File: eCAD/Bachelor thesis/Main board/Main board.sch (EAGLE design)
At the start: 65 parts, among them IC1 BC660K-GL, IC2 TP4056X, IC3 DW01A-G, IC4 ME6211C33M5G-N, IC5 ME6211C33M5G-N, IC6 ESP32-WROOM-32E_M113EH3200PH3Q, Q1 IRF7319TRPBF, Q2 IRF7319TRPBF, Q3 SI2347DS-T1-GE3, Q4 FS8205A

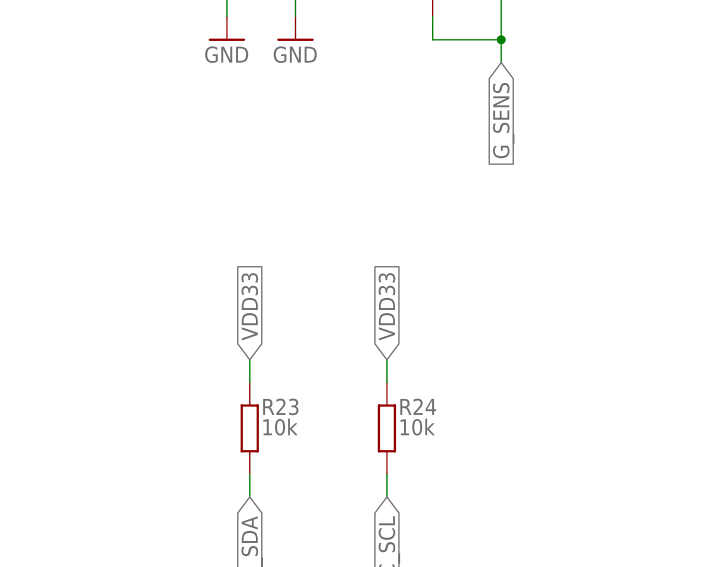
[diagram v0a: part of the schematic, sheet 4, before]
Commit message: I2C pull-up Rs added on switched source
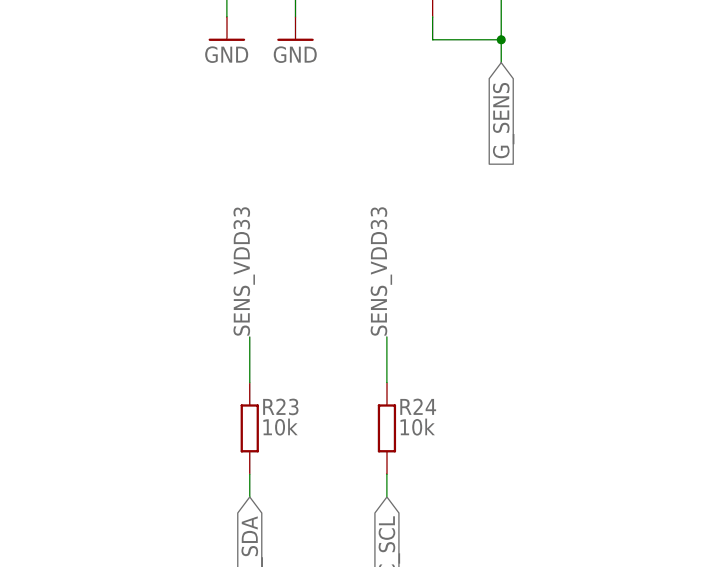
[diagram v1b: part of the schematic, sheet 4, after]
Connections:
- net SENS_VDD33: now also R23.2, R24.2
- net VDD33: no longer R23.2, R24.2
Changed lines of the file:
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@@
 <setting verticaltext="up"/>
 </settings>
-<grid distance="0.1" unitdist="inch" unit="mil" style="lines" multiple="1" display="yes" altdistance="0.01" altunitdist="inch" altunit="mil"/>
+<grid distance="0.1" unitdist="inch" unit="inch" style="lines" multiple="1" display="no" altdistance="0.01" altunitdist="inch" altunit="inch"/>
 <layers>
 <layer number="1" name="Top" color="4" fill="1" visible="no" active="no"/>
@@
 <label x="200.66" y="121.92" size="1.778" layer="95" rot="R180"/>
 </segment>
-<segment>
-<pinref part="R23" gate="G$1" pin="2"/>
-<wire x1="38.1" y1="35.56" x2="38.1" y2="38.1" width="0.1524" layer="91"/>
-<label x="38.1" y="38.1" size="1.778" layer="95" rot="R90" xref="yes"/>
-</segment>
-<segment>
-<pinref part="R24" gate="G$1" pin="2"/>
-<wire x1="53.34" y1="35.56" x2="53.34" y2="38.1" width="0.1524" layer="91"/>
-<label x="53.34" y="38.1" size="1.778" layer="95" rot="R90" xref="yes"/>
-</segment>
 </net>
 <net name="ESP_PIN" class="0">
@@
 <label x="200.66" y="78.74" size="1.778" layer="95" rot="R180"/>
 </segment>
-</net>
+<segment>
+<pinref part="R23" gate="G$1" pin="2"/>
+<wire x1="38.1" y1="35.56" x2="38.1" y2="40.64" width="0.1524" layer="91"/>
+<label x="38.1" y="40.64" size="1.778" layer="95" rot="R90"/>
+</segment>
+<segment>
+<pinref part="R24" gate="G$1" pin="2"/>
+<wire x1="53.34" y1="35.56" x2="53.34" y2="40.64" width="0.1524" layer="91"/>
+<label x="53.34" y="40.64" size="1.778" layer="95" rot="R90"/>
+</segment>
+</net>

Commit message: Work around Quectel BC660K NB-IoT module
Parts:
- removed C18: 220u, rcl:CPOL-EUD
- removed C19: 100n, rcl:C-EUC0805
- removed C20: 22p, rcl:C-EUC0805
- removed C21: 100p, rcl:C-EUC0805
- removed R25, R26: 10K, rcl:R-EU_R0805
- removed SJ5: (no value), jumper:SJ
- removed U$1: USBC-6P, USBC6P:USBC-6P
- added C12, C14, C2: 1u, rcl:C-EUC0805
- added C15, C3: 100n, rcl:C-EUC0805
- added LED1: STAT1, led:LEDCHIPLED_0805
- added Q5, Q6: IRF7319TRPBF, 1-component-search:IRF7319TRPBF
- added R1, R2: 10K, rcl:R-EU_R0805
- added R11: 100R, rcl:R-EU_R0805
- added SJ2: (no value), jumper:SJ
- added TP1, TP2: TPB2,54, testpad:TPB2,54
- added USBC: USBC-6P, USBC6P:USBC-6P
- C10: value 100n -> 10u
- C4: value 1u -> 220u; device rcl:C-EUC0805 -> rcl:CPOL-EUD
- C6: value 10u -> 22p
- C7: value 100n -> 100p
- C8, C9: value 1u -> 100n
- IC1: value BC660K-GL -> ESP32-WROOM-32E_M113EH3200PH3Q; device 1-component-search:BC660K-GL -> 1-component-search:ESP32-WROOM-32E_M113EH3200PH3Q
- IC2: value TP4056X -> BC660K-GL; device TP4056X:TP4056X -> 1-component-search:BC660K-GL
- IC4: value ME6211C33M5G-N -> TP4056X; device 1-component-search:ME6211C33M5G-N -> TP4056X:TP4056X
- IC6: value ESP32-WROOM-32E_M113EH3200PH3Q -> ME6211C33M5G-N; device 1-component-search:ESP32-WROOM-32E_M113EH3200PH3Q -> 1-component-search:ME6211C33M5G-N
- Q1, Q2: value IRF7319TRPBF -> PDTC114EU,115; device 1-component-search:IRF7319TRPBF -> PDTC114EU_115:PDTC114EU,115
- Q3: value SI2347DS-T1-GE3 -> FS8205A; device 1-component-search:SI2347DS-T1-GE3 -> 1-component-search:FS8205A
- Q4: value FS8205A -> SI2347DS-T1-GE3; device 1-component-search:FS8205A -> 1-component-search:SI2347DS-T1-GE3
- R10, R9: value 10k -> 5k1
- R12: value Rprog -> 10k
- R13: value 100R -> Rprog
- R14: value 1k -> 10k
- R18, R19: value 5k1 -> 10k
- R20: value 1M -> 10k
- R21: value 4k7 -> 10k
- R22: value 10K -> 4k7
- R5: value 10k -> 10K
- R6: value 10k -> 2k2; device rcl:R-EU_R0805 -> rcl:R-EU_R1206
- R7: value 10k -> 1M
- R8: value 10k -> 1k
- renumbered BAT_IN to JP4, C16 to C13, C17 to C1, DS18B20 to J3, ESP_BOOT1 to S2, ESP_EN1 to JP1, ESP_RESET1 to S1, FAN to JP5, I2C to J4, NB_BOOT1 to S4, NB_PSM1 to S5, NB_RESET1 to S3, R23 to R16, R24 to R17, RAIN_GAUGE to J2, SJ4 to SJ1, SOLAR_IN to J1
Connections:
- new net BOOT: IC2.BOOT
- new net N$1: IC2.DBG_RXD, TP1.TP
- new net N$16: LED1.C, R6.2
- new net N$17: Q2.OUTPUT, R6.1
- new net N$2: IC2.DBG_TXD, TP2.TP
- new net NETLIGHT: IC2.NETLIGHT, Q2.INPUT
- new net PSM_EINT: IC2.PSM_EINT
- new net RESET_N: C8.1, IC2.RESET_N, Q1.OUTPUT
- new net RESET_QUECTEL: Q1.INPUT
- net !CHRG: now also IC4.!CHRG; no longer IC2.!CHRG
- net !STDBY: now also IC4.!STDBY; no longer IC2.!STDBY
- net BAT+: now also IC4.BAT, Q4.D, Q5.S2, R11.2, R18.1; no longer IC2.BAT, Q1.S2, Q3.D, R13.2, R6.1
- net BAT-: now also C9.2, Q3.S1_1, Q3.S1_2; no longer C7.2, Q4.S1_1, Q4.S1_2
- net BOOT_N: now also IC1.IO19, R4.2; no longer IC6.IO19, R25.2
- net DS18B_SIG: now also IC1.IO32, R22.1; no longer IC6.IO32, R21.1
- net ESP_EN: now also C2.1, IC1.EN, R1.1; no longer C4.1, IC6.EN, R3.1
- net ESP_FLASH: now also IC1.IO0, R2.1; no longer IC6.IO0, R4.1
- net ESP_PIN: now also IC1.IO33, Q5.G1, Q6.G1, R14.2, R15.2; no longer IC6.IO33, Q1.G1, Q2.G1, R5.2, R9.2
- net FLASH_RX: now also IC1.RXD0; no longer IC6.RXD0
- net FLASH_TX: now also IC1.TXD0; no longer IC6.TXD0
- net GND: now also C12.2, C14.2, C15.2, C2.2, C3.1, C4.-, C5.2, C7.2, IC1.GND_1, IC1.GND_10, IC1.GND_11, IC1.GND_12, IC1.GND_2, IC1.GND_3, IC1.GND_4, IC1.GND_5, IC1.GND_6, IC1.GND_7, IC1.GND_8, IC1.GND_9, IC2.GND_1, IC2.GND_10, IC2.GND_2, IC2.GND_3, IC2.GND_4, IC2.GND_5, IC2.GND_6, IC2.GND_7, IC2.GND_8, IC2.GND_9, IC2.VIO_SEL, IC4.EAD, IC4.GND, IC4.TEMP, IC6.VSS, Q1.GND, Q2.GND, Q3.S2_1, Q3.S2_2, Q5.S1, Q6.S1, R10.1, R12.1, R13.2, R21.1, R3.1, R4.1, R7.2, USBC.GND; no longer C18.-, C19.2, C20.2, C21.2, C4.2, C5.1, C9.2, IC2.EAD, IC2.GND, IC2.TEMP, IC4.VSS, IC6.GND_1, IC6.GND_10, IC6.GND_11, IC6.GND_12, IC6.GND_2, IC6.GND_3, IC6.GND_4, IC6.GND_5, IC6.GND_6, IC6.GND_7, IC6.GND_8, IC6.GND_9, Q1.S1, Q2.S1, Q4.S2_1, Q4.S2_2, R12.2, R18.1, R19.1, R20.2, R22.1, R25.1, R26.1, U$1.GND
- net G_BAT: now also Q5.D1_2, Q5.G2, R18.2; no longer Q1.D1_2, Q1.G2, R6.2
- net G_SENS: now also Q6.D1_2, Q6.G2, R19.2; no longer Q2.D1_2, Q2.G2, R10.2
- net I2C_SCL: now also IC1.IO22; no longer IC6.IO22
- net I2C_SDA: now also IC1.IO21; no longer IC6.IO21
- net N$10: now also Q3.G1; no longer Q4.G1
- net N$11: now also R9.2, USBC.CC2; no longer R19.2, U$1.CC2
- net N$12: now also Q3.G2; no longer Q4.G2
- net N$13: now also R10.2, USBC.CC1; no longer R18.2, U$1.CC1
- net N$14: now also R7.1, USBC.S; no longer R20.1, U$1.S
- net N$15: now also Q5.D2_1, R20.2; no longer Q1.D2_1, R7.2
- net N$3: now also IC1.IO16, SJ2.1; no longer IC6.IO16, SJ3.1
- net N$4: now also IC1.IO17; no longer IC6.IO17
- net N$5: now also IC4.PROG, R13.1; no longer IC2.PROG, R12.1
- net N$7: now also C9.1, R11.1; no longer C7.1, R13.1
- net N$8: now also D1.A, SJ3.1, USBC.VBUS; no longer D2.A, SJ5.1, U$1.VBUS
- net N$9: now also R8.2; no longer R14.2
- net OUT+: now also C12.1, D2.K, IC6.CE, IC6.VIN, Q4.S; no longer C8.1, D1.K, IC4.CE, IC4.VIN, Q3.S
- net PSM_EINT_N: now also IC1.IO5, R5.2; no longer IC6.IO5, R26.2
- net RAIN_GAUGE_INPUT: now also IC1.IO4; no longer IC6.IO4
- net RAIN_SENS: now also IC1.IO35; no longer IC6.IO35
- net RESET_EN: now also IC1.IO18, R3.2; no longer IC6.IO18, R22.2
- net SENS_VDD33: now also Q6.D2_1, R22.2; no longer Q2.D2_1, R21.2
- net UART_MCU_RX: now also IC2.MAIN_TXD, SJ2.2; no longer SJ3.2
- net UART_MCU_TX: now also IC2.MAIN_RXD
- net VDD33: now also C14.1, C3.2, C4.+, C5.1, C6.1, C7.1, IC1.3V3, IC2.VBAT_1, IC2.VBAT_2, IC6.VOUT, LED1.A, Q6.S2, R1.2, R19.1, R2.2; no longer C18.+, C19.1, C20.1, C21.1, C5.2, C9.1, IC4.VOUT, IC6.3V3, Q2.S2, R10.1, R3.2, R4.2
- net VIN: now also C10.1, D1.K, D2.A, IC4.CE, IC4.VCC, Q4.G, R12.2, SJ3.2; no longer C6.1, D1.A, D2.K, IC2.CE, IC2.VCC, Q3.G, R15.2, SJ5.2
- net VOL_SENS: now also C15.1, IC1.IO34, R20.1, R21.2; no longer C10.1, IC6.IO34, R7.1, R8.2
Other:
- note added: "TVS diode?"
- note added: "VIO_SEL grounded for 3.3V logic levels"

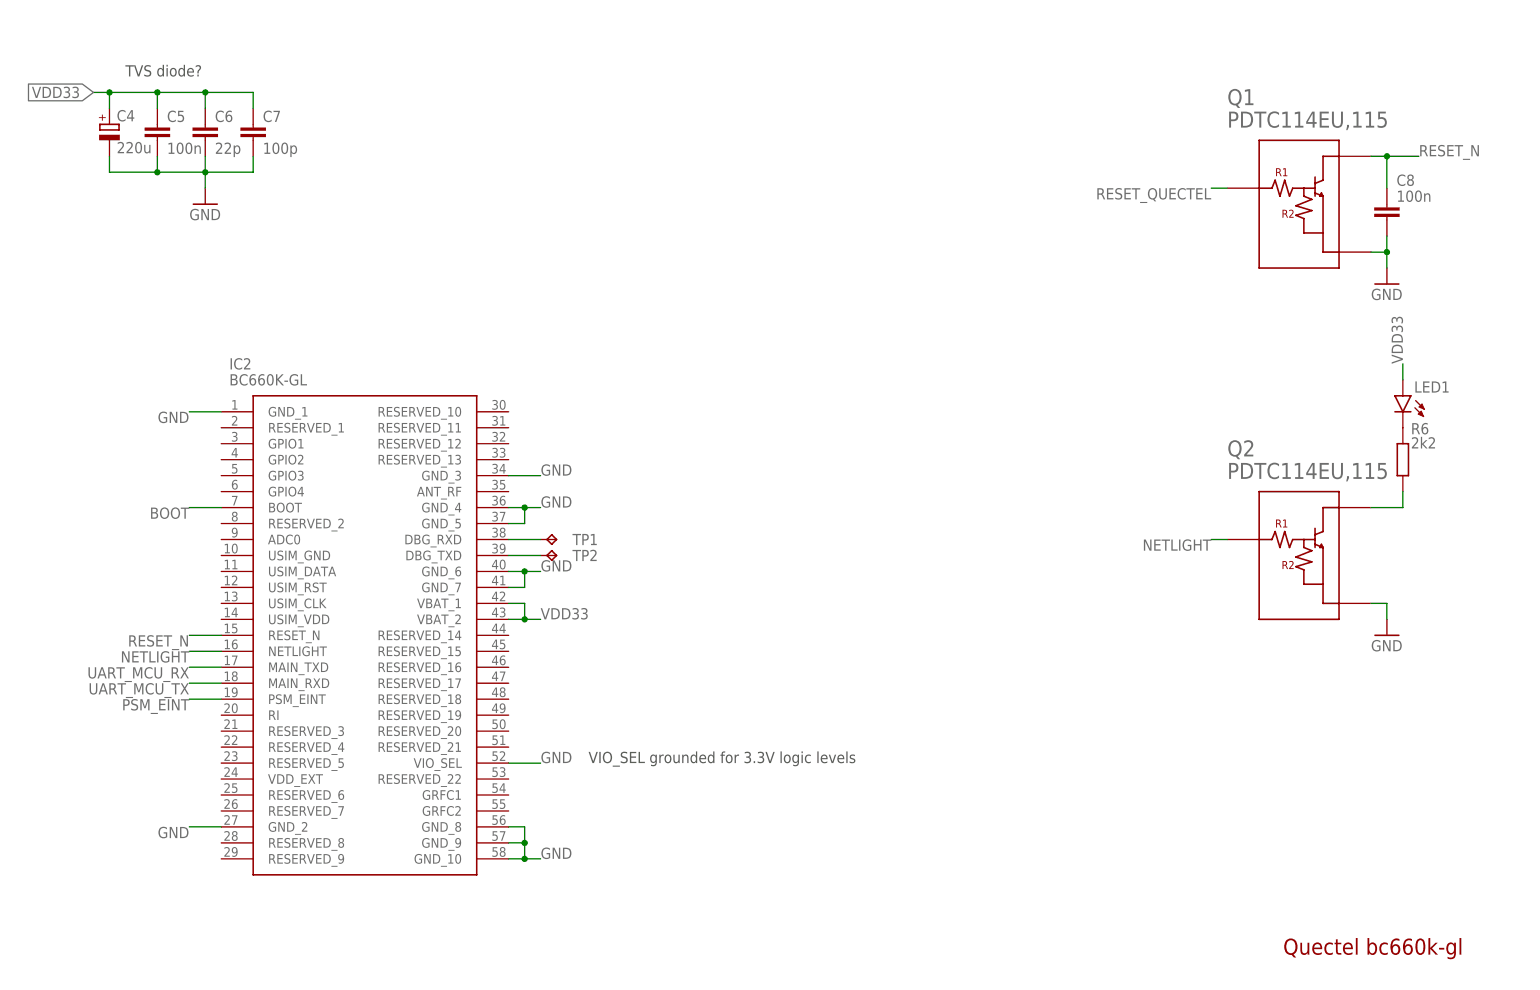
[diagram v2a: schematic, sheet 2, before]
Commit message: Work around Quectel BC660K-GL module
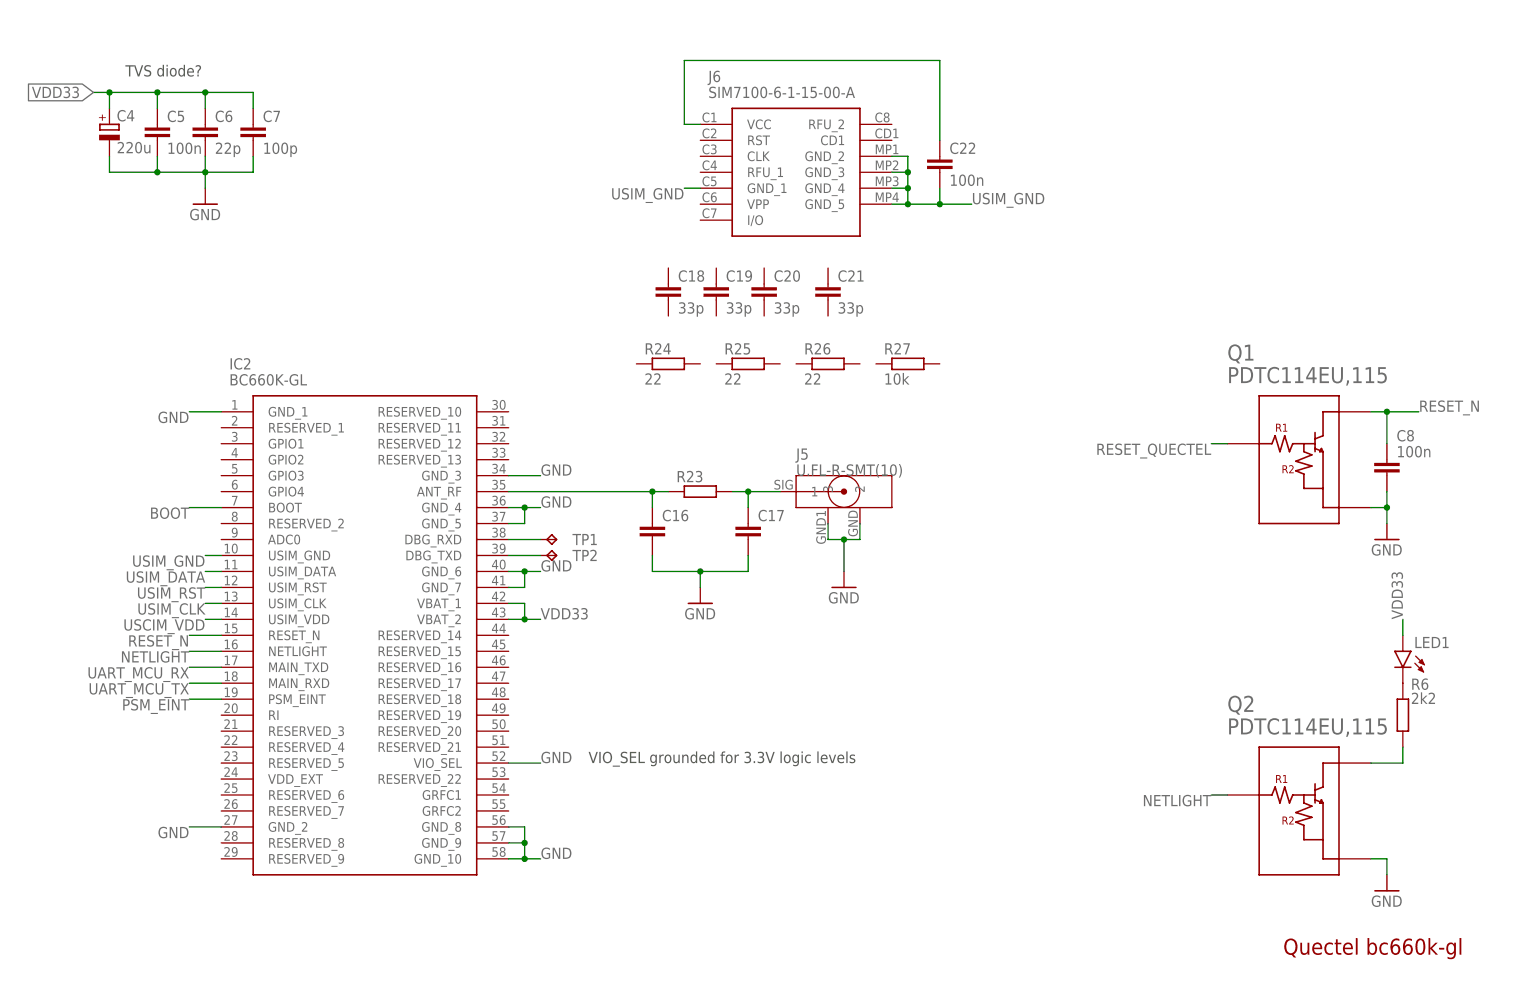
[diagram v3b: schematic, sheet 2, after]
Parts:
- added C16, C17: (no value), rcl:C-EUC0805
- added C18, C19, C20, C21: 33p, rcl:C-EUC0805
- added C22: 100n, rcl:C-EUC0805
- added J5: U.FL-R-SMT(10), Connectors:U.FL-R-SMT(10)
- added J6: SIM7100-6-1-15-00-A, 1-component-search:SIM7100-6-1-15-00-A
- added R23: (no value), rcl:R-EU_R0805
- added R24, R25, R26: 22, rcl:R-EU_R0805
- added R27: 10k, rcl:R-EU_R0805
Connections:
- new net N$18: C22.1, J6.VCC
- new net N$19: C16.1, IC2.ANT_RF, R23.1
- new net N$20: C17.1, J5.1, R23.2
- new net USCIM_VDD: IC2.USIM_VDD
- new net USIM_CLK: IC2.USIM_CLK
- new net USIM_DATA: IC2.USIM_DATA
- new net USIM_GND: C22.2, IC2.USIM_GND, J6.GND_1, J6.GND_2, J6.GND_3, J6.GND_4, J6.GND_5
- new net USIM_RST: IC2.USIM_RST
- net GND: now also C16.2, C17.2, J5.2, J5.3
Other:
- moved on the sheet: C8, LED1, Q1, Q2, R6

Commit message: Completed antena interface, power circuitry
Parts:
- removed Q5, Q6: IRF7319TRPBF, 1-component-search:IRF7319TRPBF
- removed USBC: USBC-6P, USBC6P:USBC-6P
- added $3_24_$_2023-03-17_12-09-30: USBC-6P, USBC6P:USBC-6P
- added $3_25_$_2023-03-17_12-09-30: BLOSSOM-BLM-18650-1PCS, battery-holders:BLOSSOM-BLM-18650-1PCS
- added C23: 1u, rcl:C-EUC0805
- added C24, C27, C28: 100n, rcl:C-EUC0805
- added C25: 50, rcl:CPOL-EUE5-10.5
- added C26: 22u, rcl:C-EUC0805
- added D3, D4: PMEG2010EJ,115, 1-component-search:PMEG2010EJ,115
- added D5: SMBJ6.5A, 1-component-search:SMBJ6.5A
- added HM1: BME280, 1-component-search:BME280
- added IC10, IC9: SMS3.3.TCT, 1-component-search:SMS3.3.TCT
- added IC7, IC8: ME6211C33M5G-N, 1-component-search:ME6211C33M5G-N
- added JP7: FAN, jumper:JP2E
- added LED2: !PG, led:LEDCHIPLED_0805
- added LED3: STAT2, led:LEDCHIPLED_0805
- added LED4: STAT1, led:LEDCHIPLED_0805
- added R28, R29, R33, R34, R35, R36: 10k, rcl:R-EU_R0805
- added R30, R31, R32: 4k7, rcl:R-EU_R0805
- added SJ4: (no value), jumper:SJ
- added SJ5: (no value), jumper:SJ2W
- C1, C4: value 220u -> 470u
- C10: value 10u -> 33p
- C11, C13: value 1u -> 33p
- C12: value 1u -> (none)
- C14: value 1u -> 100n
- C16: value (none) -> 100n
- C17: value (none) -> 10u
- C18, C21: value 33p -> 4u7
- C19, C20: value 33p -> 1u
- C22: value 100n -> 1u
- C8: value 100n -> 33p
- C9: value 100n -> (none)
- D1, D2: value 1N4148WS-7-F -> SMBJ6.5A; device 1-component-search:1N4148WS-7-F -> 1-component-search:SMBJ6.5A
- IC3: value DW01A-G -> SMS3.3.TCT; device 1-component-search:DW01A-G -> 1-component-search:SMS3.3.TCT
- IC4: value TP4056X -> AP9101CK6-ADTRG1; device TP4056X:TP4056X -> 1-component-search:AP9101CK6-ADTRG1
- IC5: value ME6211C33M5G-N -> FDS6898A; device 1-component-search:ME6211C33M5G-N -> 1-component-search:FDS6898A
- IC6: value ME6211C33M5G-N -> MCP73871-2CCI_ML; device 1-component-search:ME6211C33M5G-N -> 1-component-search:MCP73871-2CCI_ML
- J1: value XT30PW-M -> U.FL-R-SMT(10); device 1-component-search:XT30PW-M -> Connectors:U.FL-R-SMT(10)
- J2: value RJE01-660-01 -> SIM7100-6-1-15-00-A; device 1-component-search:RJE01-660-01 -> 1-component-search:SIM7100-6-1-15-00-A
- J3: value RJE01-660-01 -> XT30PW-M; device 1-component-search:RJE01-660-01 -> 1-component-search:XT30PW-M
- J5: value U.FL-R-SMT(10) -> RJE01-660-01; device Connectors:U.FL-R-SMT(10) -> 1-component-search:RJE01-660-01
- J6: value SIM7100-6-1-15-00-A -> RJE01-660-01; device 1-component-search:SIM7100-6-1-15-00-A -> 1-component-search:RJE01-660-01
- JP2: value UART_FLASH -> ESP_UART; device pinhead:PINHD-1X4 -> jumper:JP4E
- JP3: value UART_NB -> NB_UART; device pinhead:PINHD-1X4 -> jumper:JP4E
- JP4: value (none) -> NTC; device pinhead:PINHD-1X2 -> jumper:JP1E
- JP5: value (none) -> LED_VDD; device pinhead:PINHD-1X3 -> jumper:JP1E
- Q3: value FS8205A -> IRF7319TRPBF; device 1-component-search:FS8205A -> 1-component-search:IRF7319TRPBF
- Q4: value SI2347DS-T1-GE3 -> IRF7319TRPBF; device 1-component-search:SI2347DS-T1-GE3 -> 1-component-search:IRF7319TRPBF
- R10: value 5k1 -> (none)
- R11: value 100R -> 2k2; device rcl:R-EU_R0805 -> rcl:R-EU_R1206
- R12: value 10k -> 2k7
- R13: value Rprog -> 1M
- R14, R15: value 10k -> 5k1
- R16: value 10k -> 330R
- R17, R18, R27: value 10k -> (none)
- R19, R20, R21: value 10k -> 470
- R22: value 4k7 -> 10k
- R23: value (none) -> 10k
- R24: value 22 -> 10k
- R25: value 22 -> 1k
- R26: value 22 -> (none)
- R6: value 2k2 -> 10k; device rcl:R-EU_R1206 -> rcl:R-EU_R0805
- R7: value 1M -> 22
- R8: value 1k -> 22
- R9: value 5k1 -> 22
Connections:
- removed net !CHRG: IC4.!CHRG
- removed net !STDBY: IC4.!STDBY
- removed net N$10: IC3.OD, Q3.G1
- removed net N$11: R9.2, USBC.CC2
- removed net N$12: IC3.OC, Q3.G2
- removed net N$13: R10.2, USBC.CC1
- removed net N$14: R7.1, USBC.S
- removed net N$15: Q5.D2_1, R20.2
- removed net N$18: C22.1, J6.VCC
- removed net OUT+: C12.1, D2.K, IC6.CE, IC6.VIN, Q4.S
- removed net RAIN_SENS: IC1.IO35
- removed net RAIN_SENSE: J4.6
- removed net USCIM_VDD: IC2.USIM_VDD
- new net !PG: IC1.IO27, IC6.!PG, R19.2, R22.2
- new net !TE1: IC6.!TE, R25.1
- new net BAT_Q: Q3.D2_1, Q3.D2_2, R22.1, R23.1, R24.1, R35.2
- new net CC3: $3_24_$_2023-03-17_12-09-30.CC2, R15.1
- new net CC4: $3_24_$_2023-03-17_12-09-30.CC1, R14.1
- new net DRAIN1: IC5.D1_1, IC5.D1_2, IC5.D2_1, IC5.D2_2
- new net G3: IC4.DO, IC5.G1
- new net G4: IC4.CO, IC5.G2
- new net N$21: C10.1, IC3.I/O1, J2.RST, R7.2
- new net N$22: C11.1, IC3.I/O2, J2.CLK, R8.2
- new net N$23: C13.1, IC3.I/O4, J2.I/O, R9.2
- new net OUT: C18.1, IC6.OUT_1, IC6.OUT_2, SJ5.3
- new net PROG2: IC6.PROG3, R26.1
- new net PROG4: IC6.PROG1, R27.1
- new net PV_IN1: D1.K, D3.A, J3.1, SJ3.1
- new net S1: $3_24_$_2023-03-17_12-09-30.S, R13.1
- new net STAT1: IC1.IO25, IC6.STAT1/!LBO, R21.2, R24.2
- new net STAT2: IC1.IO26, IC6.STAT2, R20.2, R23.2
- new net THERM1: IC6.THERM, JP4.2
- new net USIM_VDD: C14.1, C8.1, IC2.USIM_VDD, IC3.I/O3, J2.VCC, R6.1
- new net VBAT: $3_25_$_2023-03-17_12-09-30.+, C21.1, D5.K, IC6.VBAT_1, IC6.VBAT_2, IC6.VBAT_SENSE, R16.2, SJ5.1
- new net VBUS1: $3_24_$_2023-03-17_12-09-30.VBUS, D2.K, D4.A, SJ4.1
- new net VCC: IC6.PROG2
- new net VDD_LED: JP5.1, LED1.A, LED2.A, LED3.A, LED4.A
- new net VIN_LDO: C20.1, IC8.CE, IC8.VIN, SJ5.2
- new net VM1: IC4.VM, R12.2
- new net VPCC1: IC6.VPCC, R17.1, R18.1
- net BAT+: now also Q3.S2, R33.1; no longer IC4.BAT, JP4.1, Q4.D, Q5.S2, R11.2, R18.1
- net BAT-: now also $3_25_$_2023-03-17_12-09-30.-, C16.2, IC4.VSS, IC5.S1; no longer C9.2, IC3.GND, JP4.2, Q3.S1_1, Q3.S1_2
- net DS18B_SIG: now also IC9.I/O4, J5.5, R32.1; no longer J3.2, R22.1
- net ESP_PIN: now also Q3.G1, Q4.G1, R28.2, R29.2; no longer Q5.G1, Q6.G1, R14.2, R15.2
- net GND: now also $3_24_$_2023-03-17_12-09-30.GND, C18.2, C19.2, C20.2, C21.2, C22.2, C23.2, C24.2, C25.-, C26.1, C27.1, C28.2, C9.2, D1.A, D2.A, D5.A, HM1.GND_1, HM1.GND_2, HM1.SDO, IC10.GND_1, IC10.GND_2, IC3.GND_1, IC3.GND_2, IC5.S2, IC6.EP, IC6.VSS_1, IC6.VSS_2, IC7.VSS, IC8.VSS, IC9.GND_1, IC9.GND_2, J3.2, J3.3, J3.4, J4.1, J4.2, J4.6, J5.4, J6.1, J6.5, J6.6, JP4.1, JP7.1, Q3.S1, Q4.S1, R14.2, R15.2, R18.2, R25.2, R26.2, R27.2, R28.1, R29.1, R36.1; no longer C14.2, C16.2, IC4.EAD, IC4.GND, IC4.TEMP, IC5.VSS, IC6.VSS, J1.4, J3.5, J5.2, J5.3, JP5.1, Q3.S2_1, Q3.S2_2, Q5.S1, Q6.S1, R10.1, R14.1, R15.1, R21.1, R7.2, R8.1, R9.1, USBC.GND
- net G_BAT: now also Q3.D1_1, Q3.D1_2, Q3.G2, R33.2; no longer Q5.D1_2, Q5.G2, R18.2
- net G_SENS: now also Q4.D1_1, Q4.D1_2, Q4.G2, R34.2; no longer Q6.D1_2, Q6.G2, R19.2
- net I2C_SCL: now also HM1.SCK, IC10.I/O1, J5.2, J6.4, R31.1; no longer J3.3, J4.3, R17.1
- net I2C_SDA: now also HM1.SDI, IC10.I/O2, J5.1, J6.3, R30.1; no longer J3.4, J4.4, R16.1
- net N$16: now also R11.2; no longer R6.2
- net N$17: now also R11.1; no longer R6.1
- net N$19: now also C9.1, R10.1; no longer C16.1, R23.1
- net N$20: now also C12.1, J1.1, R10.2; no longer C17.1, J5.1, R23.2
- net N$5: now also C16.1, IC4.VDD, R16.1; no longer IC4.PROG, R13.1
- net N$6: now also IC7.CE, JP7.2; no longer IC5.CE, JP5.2
- net N$7: now also LED2.C, R19.1; no longer C9.1, IC3.VCC, R11.1
- net N$8: now also LED3.C, R20.1; no longer D1.A, SJ3.1, USBC.VBUS
- net N$9: now also LED4.C, R21.1; no longer IC3.CS, R8.2
- net RAIN_GAUGE_INPUT: now also IC9.I/O2, J4.3; no longer J2.3
- net RESET_N: now also C15.1; no longer C8.1
- net SENS_VDD33: now also C27.2, C28.1, HM1.CSB, HM1.VDD, HM1.VDDIO, IC10.I/O3, IC10.I/O4, J5.3, J6.2, Q4.D2_1, Q4.D2_2, R30.2, R31.2, R32.2; no longer J3.1, J4.2, Q6.D2_1, R16.2, R17.2, R22.2
- net UART_MCU_RX: now also JP3.2; no longer JP3.3
- net UART_MCU_TX: now also JP3.3; no longer JP3.2
- net USIM_CLK: now also R8.1
- net USIM_DATA: now also R6.2, R9.1
- net USIM_GND: now also C14.2, J2.GND_1, J2.GND_2, J2.GND_3, J2.GND_4, J2.GND_5; no longer C22.2, J6.GND_1, J6.GND_2, J6.GND_3, J6.GND_4, J6.GND_5
- net USIM_RST: now also R7.1
- net VDD33: now also C23.1, C25.+, C26.2, IC8.VOUT, IC9.I/O1, J4.4, JP5.2, Q4.S2, R34.1; no longer C14.1, IC6.VOUT, J2.4, LED1.A, Q6.S2, R19.1
- net VDD_FAN: now also C22.1, IC7.VOUT, IC9.I/O3, J5.6; no longer C13.1, IC5.VOUT, J3.6
- net VIN: now also C17.1, C19.1, D3.K, D4.K, IC6.CE, IC6.IN_1, IC6.IN_2, IC6.SEL, IC7.VIN, JP7.3, R17.2, SJ4.2; no longer C10.1, C11.1, D1.K, D2.A, IC4.CE, IC4.VCC, IC5.VIN, J1.1, JP5.3, Q4.G, R12.2
- net VOL_SENS: now also C24.1, R35.1, R36.2; no longer C15.1, R20.1, R21.2
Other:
- note added: "I2C addr: 0x76"
- note added: "Power"
- note removed: "Charging and voltage regulation"
- note removed: "TEMP is grounded to disable temperature riden stop charge"
- note removed: "TVS diode?"
